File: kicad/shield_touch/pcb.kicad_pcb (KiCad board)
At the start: 2 copper layers, 37.6 x 35.1 mm, 22 parts, among them J1 Conn_01x12_Fem_l, J2 Conn_01x12_Fem_r, J3 Conn_01x09_Fem_b_l, J4 Conn_01x11_Fem_b_r_touch

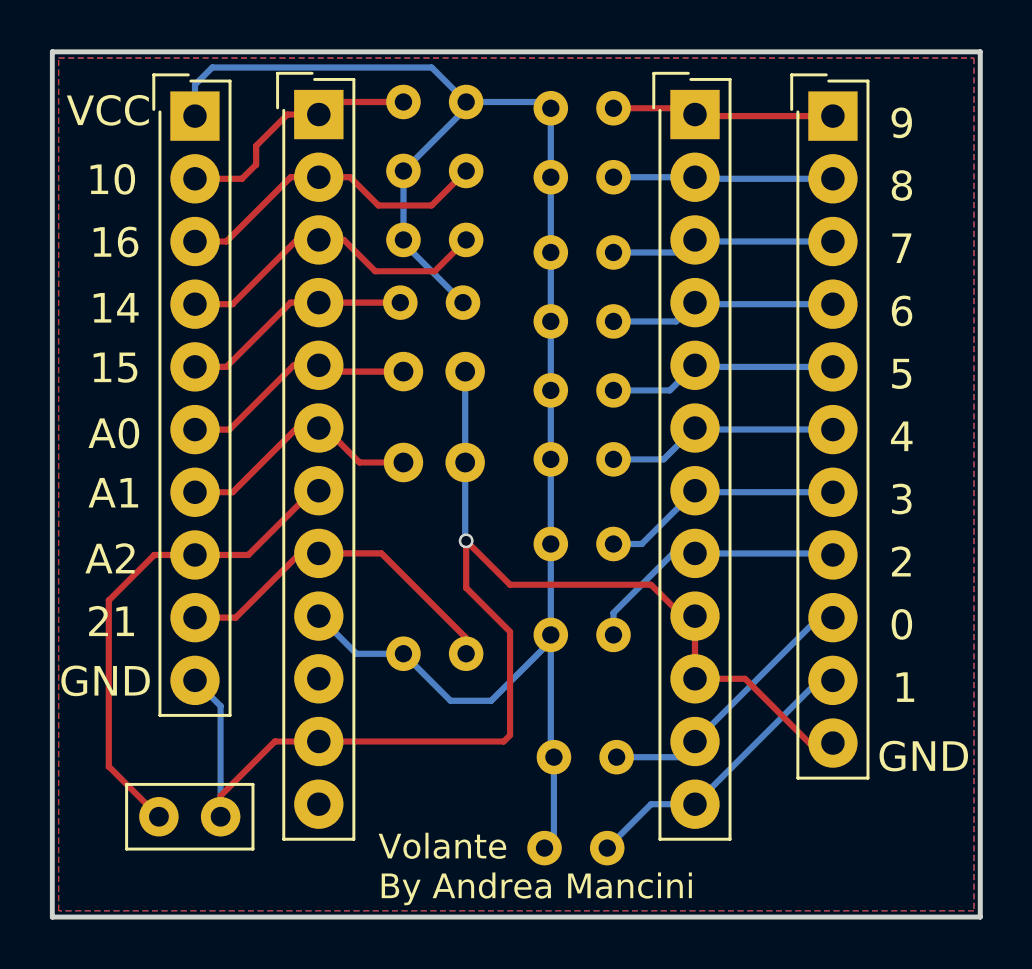
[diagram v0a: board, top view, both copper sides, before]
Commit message: update
- resistors on front side pcb
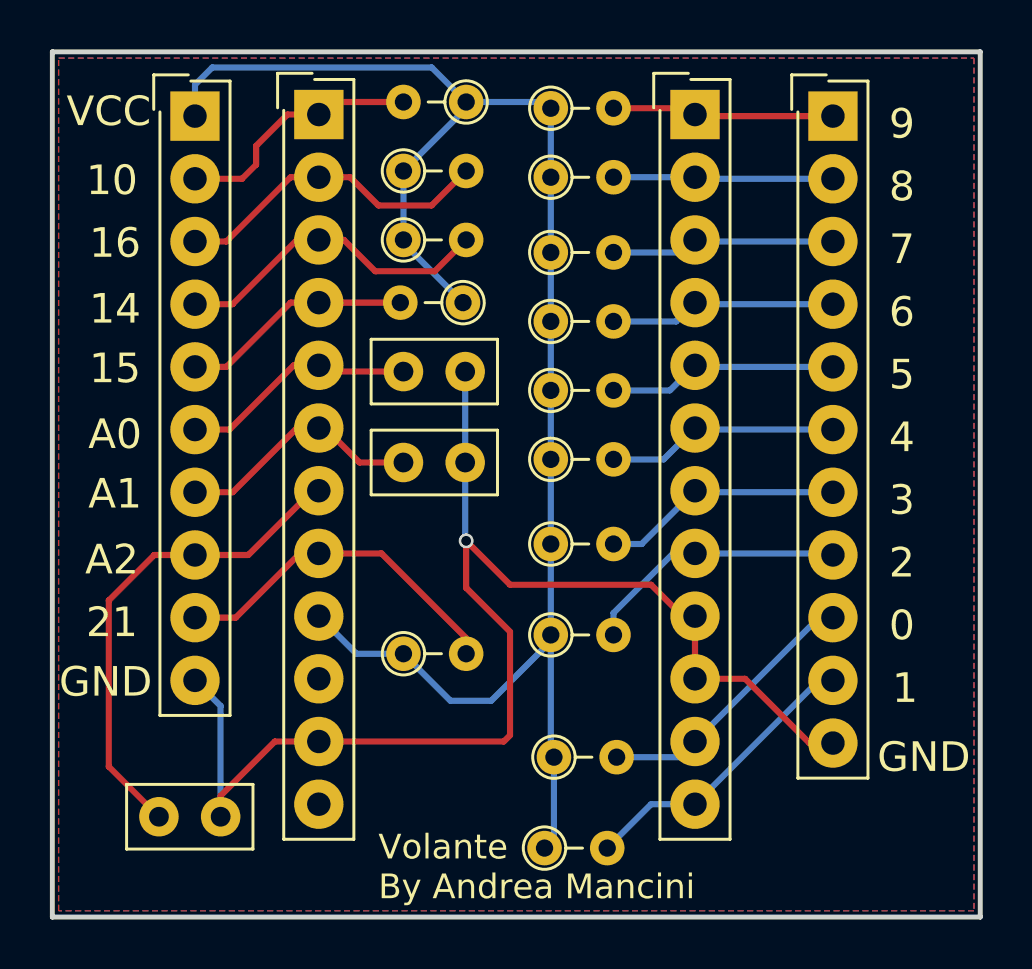
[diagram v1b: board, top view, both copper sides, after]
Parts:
- C1, C2, R1, R10, R11, R12, R13, R14, R15, R2, R3, R4, R5, R6, R7, R8, R9: moved to F.Cu
